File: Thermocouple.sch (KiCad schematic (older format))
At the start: 14 parts

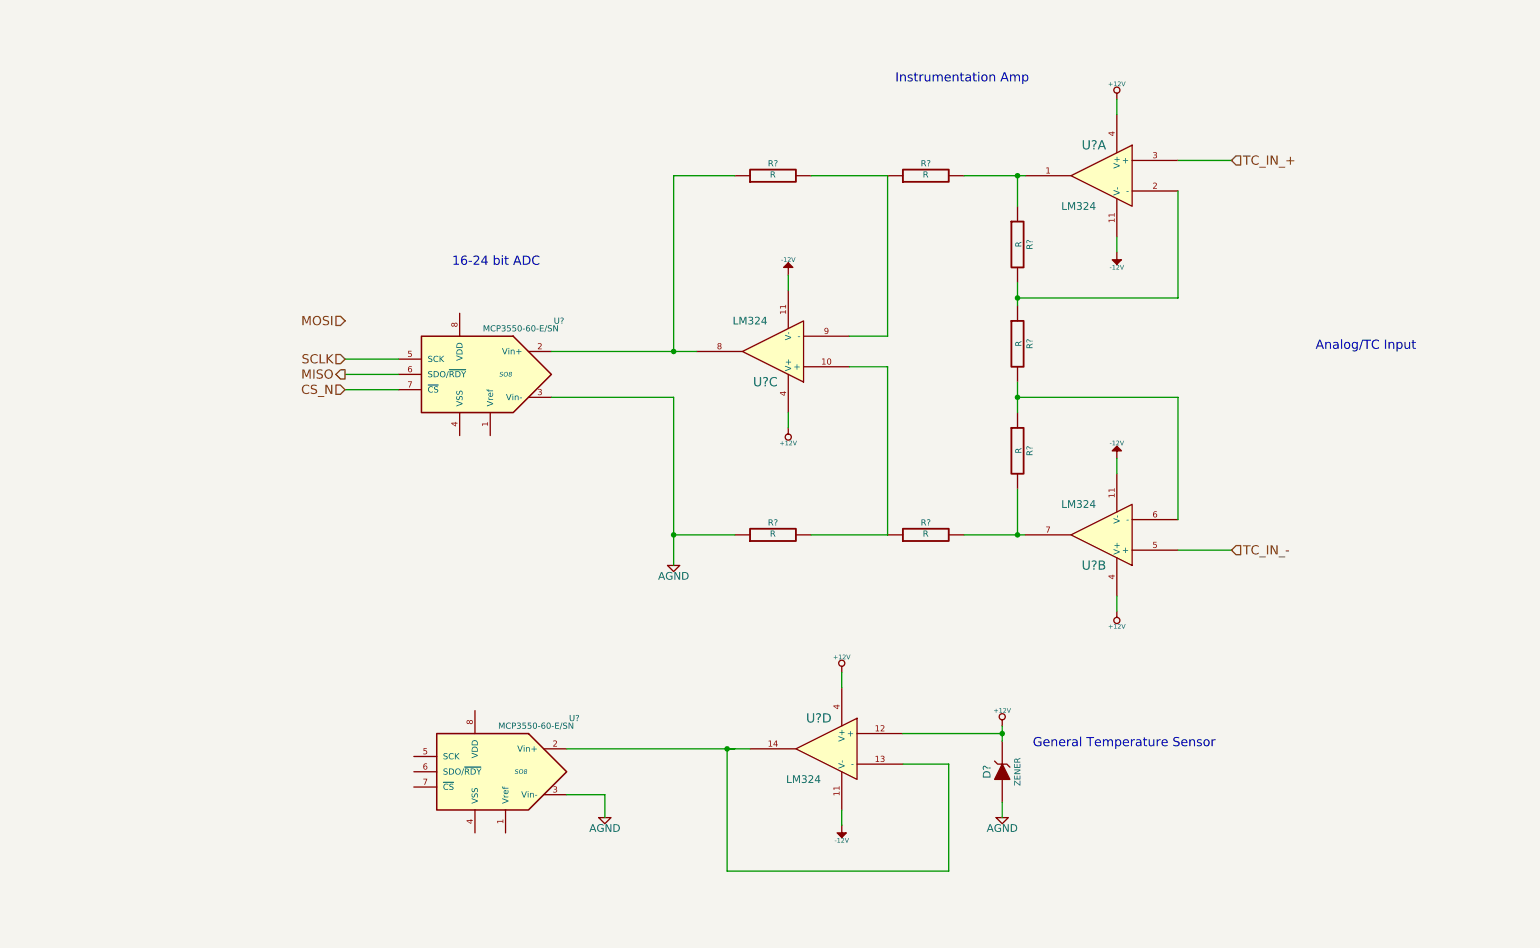
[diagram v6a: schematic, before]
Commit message: RELAY 02-20-2014
1) Created and associated footprints for relay module
2) Placed relay module's components in PCB layout
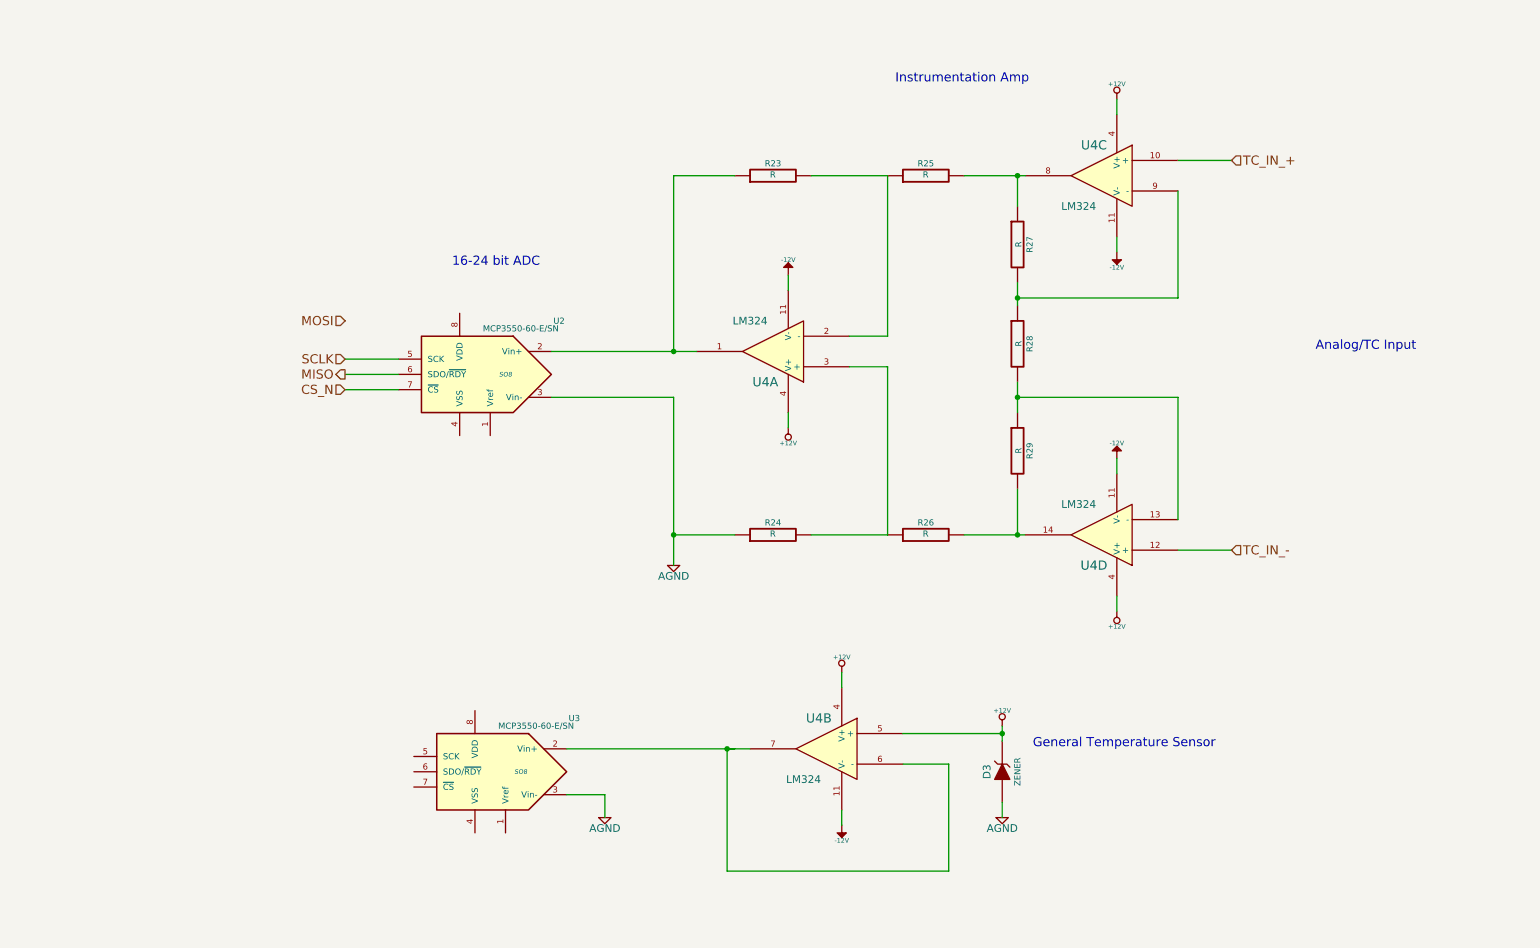
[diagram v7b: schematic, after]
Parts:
- gave numbers to parts that had none: 11
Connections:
- net +12V: now also U4.5 (+); no longer U4.12 (+)
- net TC_IN_+: now also U4.10 (+); no longer U4.3 (+)
- net TC_IN_-: now also U4.12 (+); no longer U4.5 (+)
- net at R25.2, R27.1: now also U4.8; no longer U4.1
- net at R27.2, R28.1: now also U4.9 (-); no longer U4.2 (-)
- net at R28.2, R29.1: now also U4.13 (-); no longer U4.6 (-)
- net at R26.2, R29.2: now also U4.14; no longer U4.7
- net at R24.2, R26.1: now also U4.3 (+); no longer U4.10 (+)
- net at R23.1, U2.2 (Vin+): now also U4.1; no longer U4.8
- net at R23.2, R25.1: now also U4.2 (-); no longer U4.9 (-)
- new net: U3.2 (Vin+), U4.6 (-), U4.7
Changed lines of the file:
@@
 Sheet 3 9
 Title ""
-Date "11 feb 2014"
+Date "20 feb 2014"
 Rev ""
 Comp ""
@@
 CS_N
 $Comp
-L LM324 U?
-U 1 1 52F4A11F
+L LM324 U4
+U 3 1 52F4A11F
 P 7600 2050
-F 0 "U?" H 7650 2250 60  0000 C CNN
+F 0 "U4" H 7650 2250 60  0000 C CNN
 F 1 "LM324" H 7750 1850 50  0000 C CNN
 F 2 "~" H 7600 2050 60  0000 C CNN
 F 3 "~" H 7600 2050 60  0000 C CNN
-	1    7600 2050
+	3    7600 2050
 	-1   0    0    -1
 $EndComp
 $Comp
-L LM324 U?
-U 2 1 52F4A136
+L LM324 U4
+U 4 1 52F4A136
 P 7600 4400
-F 0 "U?" H 7650 4600 60  0000 C CNN
+F 0 "U4" H 7650 4600 60  0000 C CNN
 F 1 "LM324" H 7750 4200 50  0000 C CNN
 F 2 "~" H 7600 4400 60  0000 C CNN
 F 3 "~" H 7600 4400 60  0000 C CNN
-	2    7600 4400
+	4    7600 4400
 	-1   0    0    1
 $EndComp
 $Comp
-L LM324 U?
-U 3 1 52F4A13C
+L LM324 U4
+U 1 1 52F4A13C
 P 5450 3200
-F 0 "U?" H 5500 3400 60  0000 C CNN
+F 0 "U4" H 5500 3400 60  0000 C CNN
 F 1 "LM324" H 5600 3000 50  0000 C CNN
 F 2 "~" H 5450 3200 60  0000 C CNN
 F 3 "~" H 5450 3200 60  0000 C CNN
-	3    5450 3200
+	1    5450 3200
 	-1   0    0    1
 $EndComp
 $Comp
-L LM324 U?
-U 4 1 52F4A142
+L LM324 U4
+U 2 1 52F4A142
 P 5800 5800
-F 0 "U?" H 5850 6000 60  0000 C CNN
+F 0 "U4" H 5850 6000 60  0000 C CNN
 F 1 "LM324" H 5950 5600 50  0000 C CNN
 F 2 "~" H 5800 5800 60  0000 C CNN
 F 3 "~" H 5800 5800 60  0000 C CNN
-	4    5800 5800
+	2    5800 5800
 	-1   0    0    -1
 $EndComp
 $Comp
-L R R?
+L R R28
 U 1 1 52F4A190
 P 7050 3150
-F 0 "R?" V 7130 3150 40  0000 C CNN
+F 0 "R28" V 7130 3150 40  0000 C CNN
 F 1 "R" V 7057 3151 40  0000 C CNN
 F 2 "~" V 6980 3150 30  0000 C CNN
@@
 $EndComp
 $Comp
-L R R?
+L R R27
 U 1 1 52F4A1B6
 P 7050 2500
-F 0 "R?" V 7130 2500 40  0000 C CNN
+F 0 "R27" V 7130 2500 40  0000 C CNN
 F 1 "R" V 7057 2501 40  0000 C CNN
 F 2 "~" V 6980 2500 30  0000 C CNN
@@
 $EndComp
 $Comp
-L R R?
+L R R29
 U 1 1 52F4A1C1
 P 7050 3850
-F 0 "R?" V 7130 3850 40  0000 C CNN
+F 0 "R29" V 7130 3850 40  0000 C CNN
 F 1 "R" V 7057 3851 40  0000 C CNN
 F 2 "~" V 6980 3850 30  0000 C CNN
@@
 Connection ~ 7050 3500
 $Comp
-L R R?
+L R R26
 U 1 1 52F4A22A
 P 6450 4400
-F 0 "R?" V 6530 4400 40  0000 C CNN
+F 0 "R26" V 6530 4400 40  0000 C CNN
 F 1 "R" V 6457 4401 40  0000 C CNN
 F 2 "~" V 6380 4400 30  0000 C CNN
@@
 $EndComp
 $Comp
-L R R?
+L R R25
 U 1 1 52F4A230
 P 6450 2050
-F 0 "R?" V 6530 2050 40  0000 C CNN
+F 0 "R25" V 6530 2050 40  0000 C CNN
 F 1 "R" V 6457 2051 40  0000 C CNN
 F 2 "~" V 6380 2050 30  0000 C CNN
@@
 $EndComp
 $Comp
-L R R?
+L R R24
 U 1 1 52F4A238
 P 5450 4400
-F 0 "R?" V 5530 4400 40  0000 C CNN
+F 0 "R24" V 5530 4400 40  0000 C CNN
 F 1 "R" V 5457 4401 40  0000 C CNN
 F 2 "~" V 5380 4400 30  0000 C CNN
@@
 $EndComp
 $Comp
-L R R?
+L R R23
 U 1 1 52F4A23E
 P 5450 2050
-F 0 "R?" V 5530 2050 40  0000 C CNN
+F 0 "R23" V 5530 2050 40  0000 C CNN
 F 1 "R" V 5457 2051 40  0000 C CNN
 F 2 "~" V 5380 2050 30  0000 C CNN
@@
 	8450 4500 8100 4500
 $Comp
-L -12V #PWR?
+L -12V #PWR14
 U 1 1 52F4A344
 P 7700 2550
-F 0 "#PWR?" H 7700 2680 20  0001 C CNN
+F 0 "#PWR14" H 7700 2680 20  0001 C CNN
 F 1 "-12V" H 7700 2650 30  0000 C CNN
 F 2 "" H 7700 2550 60  0000 C CNN
@@
 $EndComp
 $Comp
-L -12V #PWR?
+L -12V #PWR15
 U 1 1 52F4A351
 P 7700 3900
-F 0 "#PWR?" H 7700 4030 20  0001 C CNN
+F 0 "#PWR15" H 7700 4030 20  0001 C CNN
 F 1 "-12V" H 7700 4000 30  0000 C CNN
 F 2 "" H 7700 3900 60  0000 C CNN
@@
 $EndComp
 $Comp
-L -12V #PWR?
+L -12V #PWR7
 U 1 1 52F4A357
 P 5550 2700
-F 0 "#PWR?" H 5550 2830 20  0001 C CNN
+F 0 "#PWR7" H 5550 2830 20  0001 C CNN
 F 1 "-12V" H 5550 2800 30  0000 C CNN
 F 2 "" H 5550 2700 60  0000 C CNN
@@
 $EndComp
 $Comp
-L +12V #PWR?
+L +12V #PWR13
 U 1 1 52F4A36D
 P 7700 1550
-F 0 "#PWR?" H 7700 1500 20  0001 C CNN
+F 0 "#PWR13" H 7700 1500 20  0001 C CNN
 F 1 "+12V" H 7700 1650 30  0000 C CNN
 F 2 "" H 7700 1550 60  0000 C CNN
@@
 $EndComp
 $Comp
-L +12V #PWR?
+L +12V #PWR8
 U 1 1 52F4A37C
 P 5550 3700
-F 0 "#PWR?" H 5550 3650 20  0001 C CNN
+F 0 "#PWR8" H 5550 3650 20  0001 C CNN
 F 1 "+12V" H 5550 3800 30  0000 C CNN
 F 2 "" H 5550 3700 60  0000 C CNN
@@
 	7700 2450 7700 2550
 $Comp
-L +12V #PWR?
+L +12V #PWR11
 U 1 1 52F4A455
 P 6950 5650
-F 0 "#PWR?" H 6950 5600 20  0001 C CNN
+F 0 "#PWR11" H 6950 5600 20  0001 C CNN
 F 1 "+12V" H 6950 5750 30  0000 C CNN
 F 2 "" H 6950 5650 60  0000 C CNN
@@
 	7700 4800 7700 4900
 $Comp
-L AGND #PWR?
+L AGND #PWR6
 U 1 1 52F4A486
 P 4800 4600
-F 0 "#PWR?" H 4800 4600 40  0001 C CNN
+F 0 "#PWR6" H 4800 4600 40  0001 C CNN
 F 1 "AGND" H 4800 4530 50  0000 C CNN
 F 2 "" H 4800 4600 60  0000 C CNN
@@
 	4800 4400 5200 4400
 $Comp
-L MCP3550-60-E/SN U?
+L MCP3550-60-E/SN U2
 U 1 1 52F4A4C5
 P 3500 3350
-F 0 "U?" H 2950 3700 40  0000 C CNN
+F 0 "U2" H 2950 3700 40  0000 C CNN
 F 1 "MCP3550-60-E/SN" H 3200 3650 40  0000 C CNN
 F 2 "SO8" H 3300 3350 30  0000 C CIN
@@
 	3000 3350 2650 3350
 $Comp
-L ZENER D?
+L ZENER D3
 U 1 1 52F4A5B3
 P 6950 5950
-F 0 "D?" H 6950 6050 50  0000 C CNN
+F 0 "D3" H 6950 6050 50  0000 C CNN
 F 1 "ZENER" H 6950 5850 40  0000 C CNN
 F 2 "~" H 6950 5950 60  0000 C CNN
@@
 	6950 5650 6950 5750
 $Comp
-L AGND #PWR?
+L AGND #PWR12
 U 1 1 52F4A5F2
 P 6950 6250
-F 0 "#PWR?" H 6950 6250 40  0001 C CNN
+F 0 "#PWR12" H 6950 6250 40  0001 C CNN
 F 1 "AGND" H 6950 6180 50  0000 C CNN
 F 2 "" H 6950 6250 60  0000 C CNN
@@
 	5150 5800 5300 5800
 $Comp
-L MCP3550-60-E/SN U?
+L MCP3550-60-E/SN U3
 U 1 1 52F4A684
 P 3600 5950
-F 0 "U?" H 3050 6300 40  0000 C CNN
+F 0 "U3" H 3050 6300 40  0000 C CNN
 F 1 "MCP3550-60-E/SN" H 3300 6250 40  0000 C CNN
 F 2 "SO8" H 3400 5950 30  0000 C CIN
@@
 	4100 5800 5200 5800
 $Comp
-L AGND #PWR?
+L AGND #PWR5
 U 1 1 52F4A6BB
 P 4350 6250
-F 0 "#PWR?" H 4350 6250 40  0001 C CNN
+F 0 "#PWR5" H 4350 6250 40  0001 C CNN
 F 1 "AGND" H 4350 6180 50  0000 C CNN
 F 2 "" H 4350 6250 60  0000 C CNN
@@
 16-24 bit ADC
 $Comp
-L +12V #PWR?
+L +12V #PWR16
 U 1 1 52F82613
 P 7700 4900
-F 0 "#PWR?" H 7700 4850 20  0001 C CNN
+F 0 "#PWR16" H 7700 4850 20  0001 C CNN
 F 1 "+12V" H 7700 5000 30  0000 C CNN
 F 2 "" H 7700 4900 60  0000 C CNN
@@
 $EndComp
 $Comp
-L +12V #PWR?
+L +12V #PWR9
 U 1 1 52F827D8
 P 5900 5300
-F 0 "#PWR?" H 5900 5250 20  0001 C CNN
+F 0 "#PWR9" H 5900 5250 20  0001 C CNN
 F 1 "+12V" H 5900 5400 30  0000 C CNN
 F 2 "" H 5900 5300 60  0000 C CNN
@@
 $EndComp
 $Comp
-L -12V #PWR?
+L -12V #PWR10
 U 1 1 52F827DE
 P 5900 6300
-F 0 "#PWR?" H 5900 6430 20  0001 C CNN
+F 0 "#PWR10" H 5900 6430 20  0001 C CNN
 F 1 "-12V" H 5900 6400 30  0000 C CNN
 F 2 "" H 5900 6300 60  0000 C CNN

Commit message: THERMOCOUPLE 02-22-2014
Associated and placed PCB footprints of thermocouple modules in layout
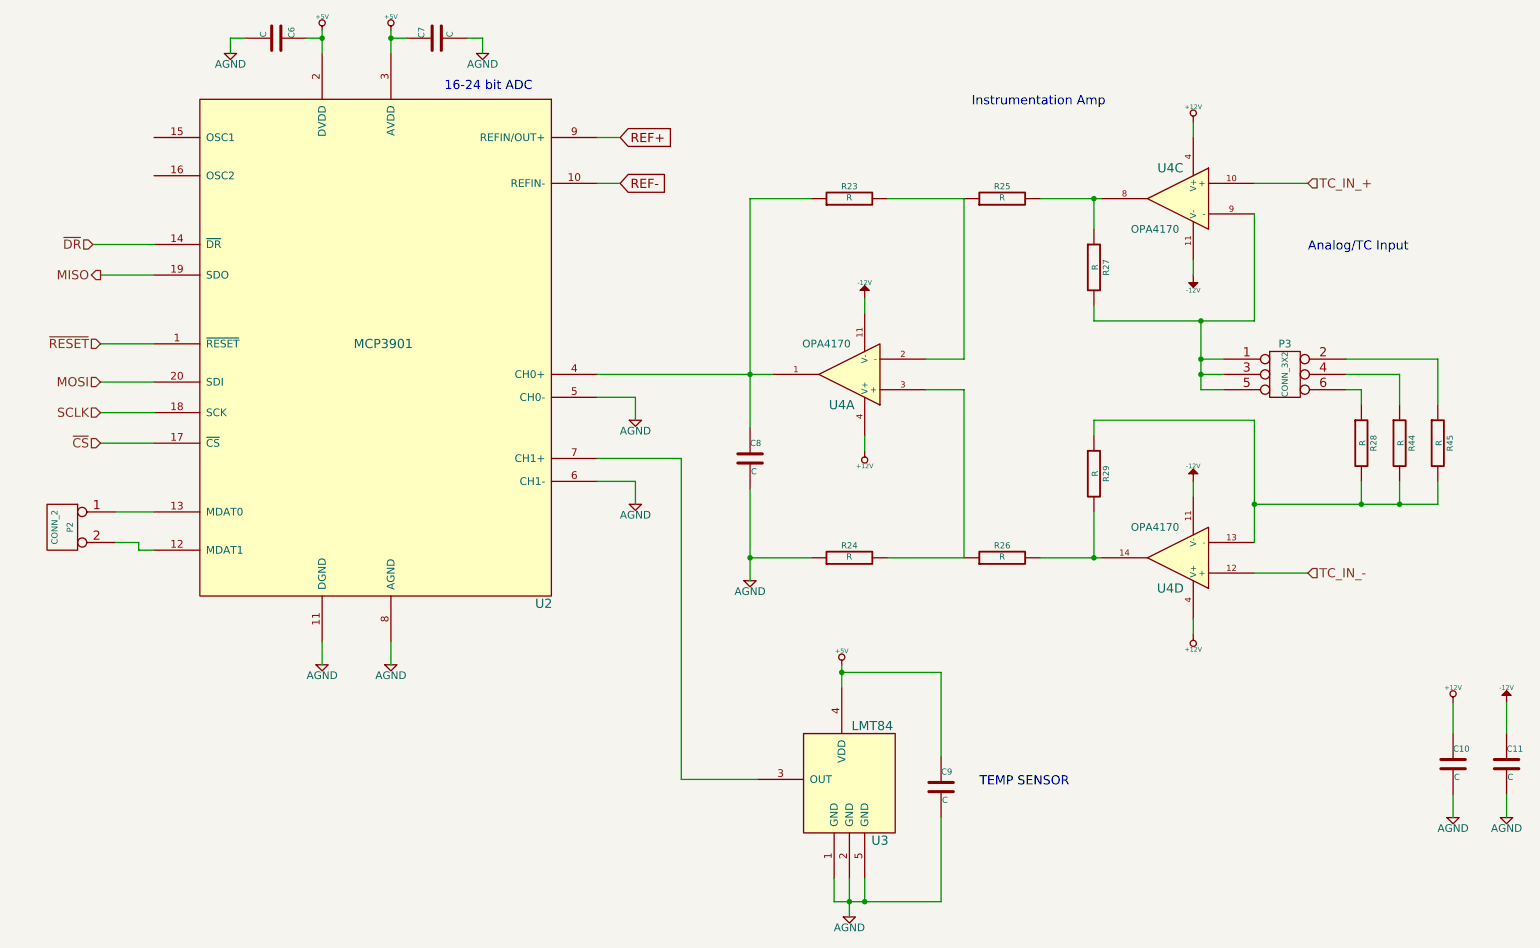
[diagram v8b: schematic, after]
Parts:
- removed D3: ZENER, ~, symbol ZENER
- removed U2, U3: MCP3550-60-E/SN, SO8, symbol MCP3550-60-E/SN
- removed unit 2 of U4
- added C10, C11, C6, C7, C8, C9: C, ~, symbol C
- added P2: CONN_2, symbol CONN_2
- added P3: CONN_3X2, symbol CONN_3X2
- added R44, R45: R, ~, symbol R
- added U2: MCP3901, symbol MCP3901
- added U3: LMT84, symbol LMT84
- U4: value LM324 -> OPA4170
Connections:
- net +12V: now also C10.1
- net -12V: now also C11.1
- net AGND: now also C10.2, C11.2, C6.2, C7.2, C8.2, C9.2, U2.11 (DGND), U2.5 (CH0-), U2.6 (CH1-), U2.8 (AGND), U3.1 (GND), U3.2 (GND), U3.5 (GND)
- net MISO: now also U2.19 (SDO)
- net MOSI: now also U2.20 (SDI)
- net SCLK: now also U2.18 (SCK)
- net at R27.2, U4.9 (-): now also P3.1, P3.3, P3.5; no longer R28.1
- net at R28.2, R29.1, U4.13 (-): now also R44.2, R45.2
- net at R23.1, U4.1: now also C8.1, U2.4 (CH0+)
- new net: P3.6, R28.1
- new net: P2.2 (PM), U2.12 (MDAT1)
- new net: P2.1 (P1), U2.13 (MDAT0)
- new net: U2.7 (CH1+), U3.3 (OUT)
- new net: P3.2, R45.1
- new net: P3.4, R44.1
- new net +5V: C6.1, C7.1, C9.1, U2.2 (DVDD), U2.3 (AVDD), U3.4 (VDD)
- new net REF+: U2.9 (REFIN/OUT+)
- new net REF-: U2.10 (REFIN-)
- new net ~CS: U2.17 (~CS)
- new net ~DR: U2.14 (~DR)
- new net ~RESET: U2.1 (~RESET)
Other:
- note added: "TEMP SENSOR"
- note removed: "General Temperature Sensor"
- moved on the sheet: R23, R24, R25, R26, R27, R28, R29, U4A, U4C, U4D
